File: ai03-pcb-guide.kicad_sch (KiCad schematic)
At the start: 16 parts, among them J1 Conn_01x04_Socket, J2 AVR-ISP-6, U1 ATmega32U4-A, Y1 16MHz

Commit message: more tracing work
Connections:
- net Col 11: now also U1.12 (PB7); no longer U1.25 (PD4)
- net Col 12: now also U1.25 (PD4); no longer U1.26 (PD6)
- net Col 13: now also U1.26 (PD6); no longer U1.27 (PD7)
- net Col 14: now also U1.27 (PD7); no longer U1.28 (PB4)
- net Col 2: now also U1.31 (PC6); no longer U1.12 (PB7)
- net Col 3: now also U1.32 (PC7); no longer U1.31 (PC6)
- net Col 4: now also U1.28 (PB4); no longer U1.32 (PC7)

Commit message: most wiring complete
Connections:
- net Col 0: now also U1.28 (PB4); no longer U1.29 (PB5)
- net Col 1: now also U1.29 (PB5); no longer U1.30 (PB6)
- net Col 10: now also U1.12 (PB7); no longer U1.21 (PD3)
- net Col 11: now also U1.18 (PD0); no longer U1.12 (PB7)
- net Col 12: now also U1.19 (PD1); no longer U1.25 (PD4)
- net Col 13: now also U1.21 (PD3); no longer U1.26 (PD6)
- net Col 14: now also U1.25 (PD4); no longer U1.27 (PD7)
- net Col 2: now also U1.30 (PB6); no longer U1.31 (PC6)
- net Col 3: now also U1.31 (PC6); no longer U1.32 (PC7)
- net Col 4: now also U1.32 (PC7); no longer U1.28 (PB4)
- net Col 5: now also U1.26 (PD6); no longer U1.36 (PF7)
- net Col 6: now also U1.27 (PD7); no longer U1.8 (PB0)
- net Col 7: now also U1.41 (PF0); no longer J2.1 (MISO), U1.11 (PB3)
- net Col 8: now also U1.8 (PB0); no longer U1.18 (PD0)
- net Col 9: now also J2.1 (MISO), U1.11 (PB3); no longer U1.19 (PD1)
- net Row 0: now also U1.38 (PF5); no longer U1.1 (PE6)
- net Row 1: now also U1.39 (PF4); no longer U1.37 (PF6)
- net Row 2: now also U1.40 (PF1); no longer U1.38 (PF5)
- net Row 3: now also U1.1 (PE6); no longer U1.39 (PF4)
- net Row 4: now also U1.37 (PF6); no longer U1.40 (PF1)
- net Row 5: now also U1.36 (PF7); no longer U1.41 (PF0)

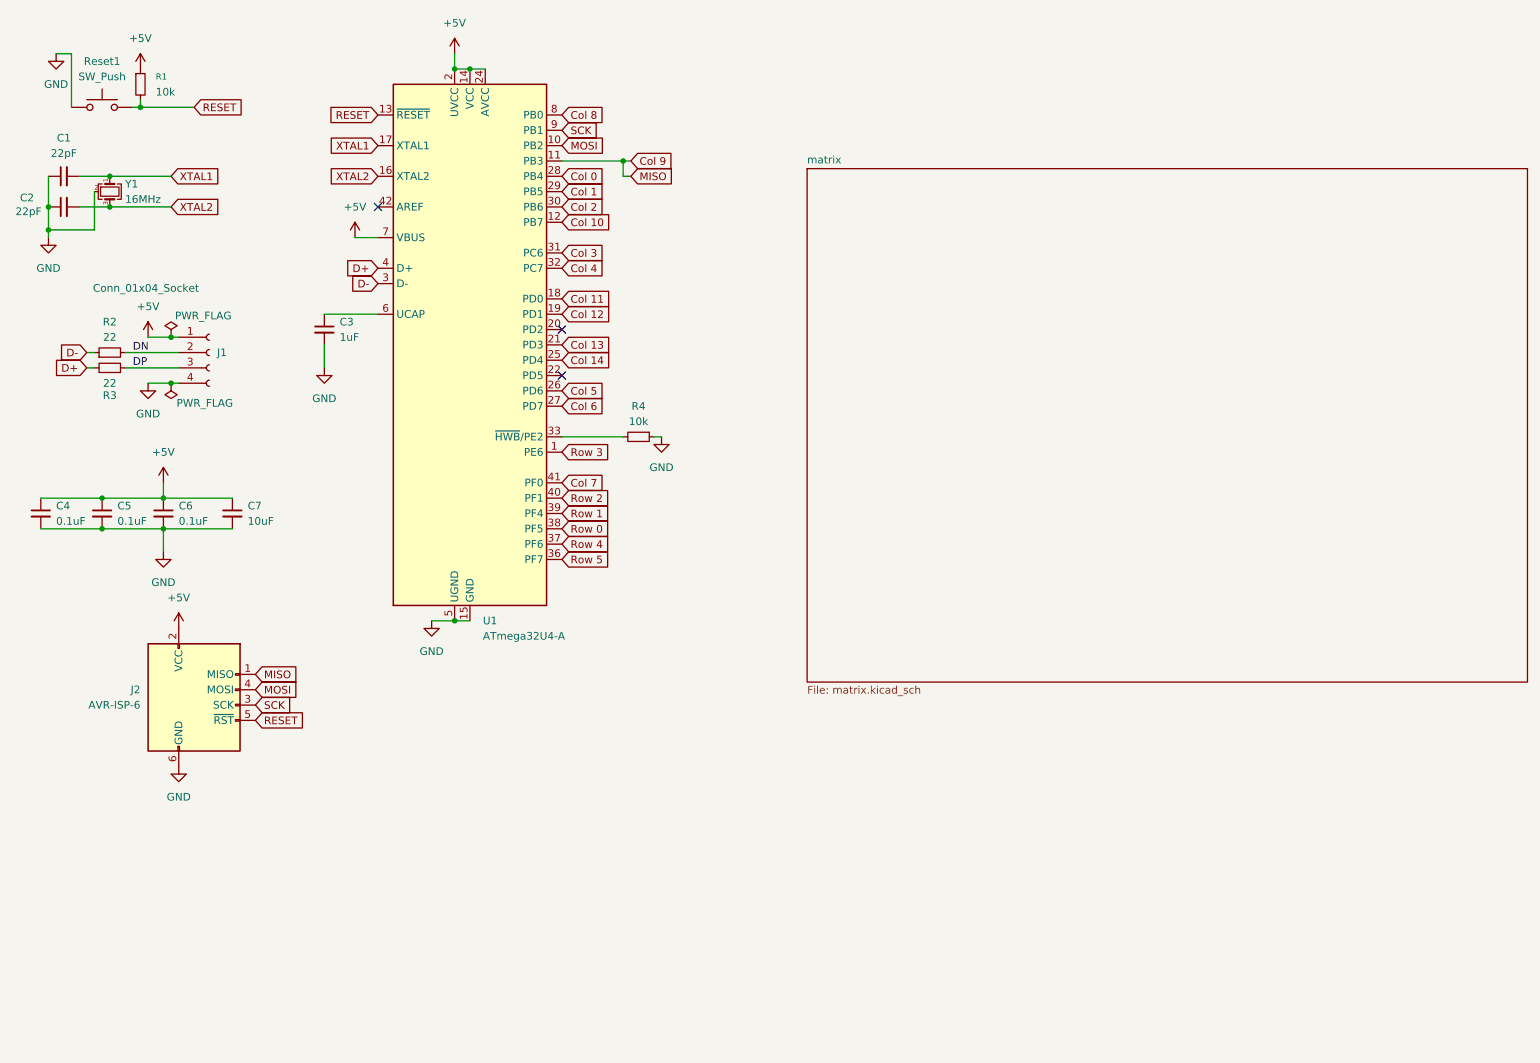
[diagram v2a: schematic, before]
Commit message: added trackpoint wiring
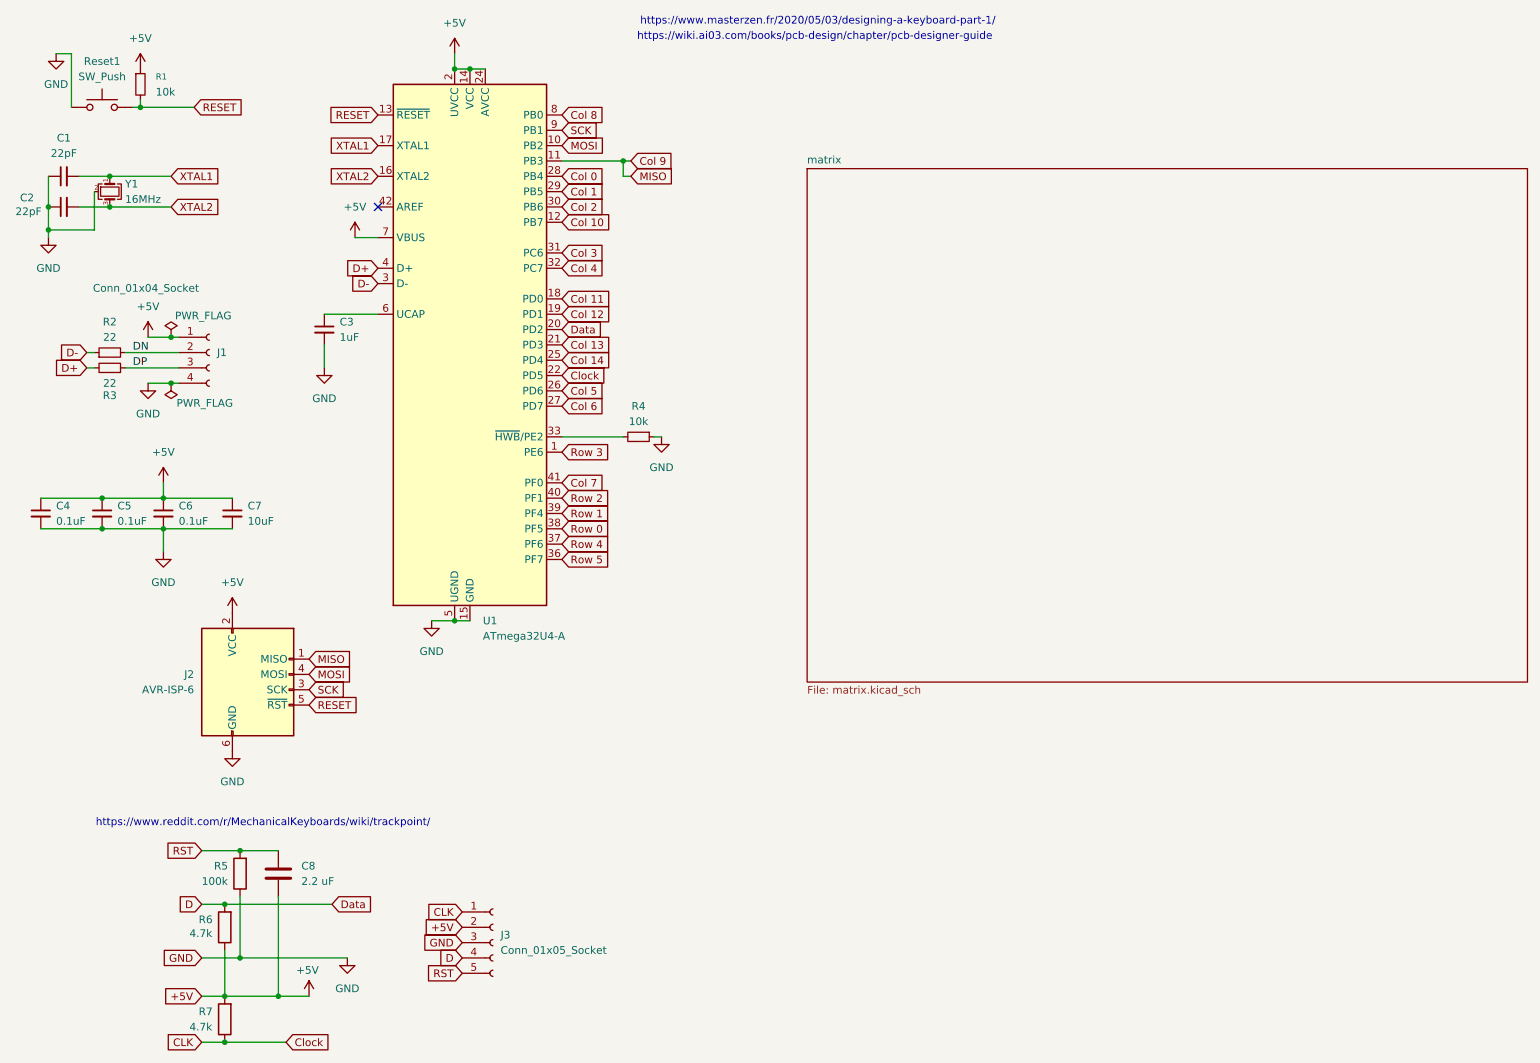
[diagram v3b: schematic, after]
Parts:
- added C8: 2.2 uF, Capacitor_SMD:C_0805_2012Metric, symbol Device:C
- added J3: Conn_01x05_Socket, Connector_Molex:Molex_Pico-EZmate_78171-0005_1x05-1MP_P1.20mm_Vertical, symbol Connector:Conn_01x05_Socket
- added R5: 100k, Resistor_SMD:R_0805_2012Metric, symbol Device:R
- added R6, R7: 4.7k, Resistor_SMD:R_0805_2012Metric, symbol Device:R
- C7: footprint Resistor_SMD:R_0805_2012Metric -> Capacitor_SMD:C_0805_2012Metric
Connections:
- net +5V: now also C8.2, J3.2 (Pin_2), R6.1, R7.2
- net GND: now also J3.3 (Pin_3), R5.1
- net D: now reaches U1.20 (PD2)
- net D: now also J3.4 (Pin_4), R6.2
- net CLK: now reaches U1.22 (PD5)
- net CLK: now also J3.1 (Pin_1), R7.1
- new net RST: C8.1, J3.5 (Pin_5), R5.2
- no-connect marks 3 -> 1
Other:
- note added: "https://wiki.ai03.com/books/pcb-design/chapter/pcb-designer-guide"
- note added: "https://www.masterzen.fr/2020/05/03/designing-a-keyboard-part-1/"
- note added: "https://www.reddit.com/r/MechanicalKeyboards/wiki/trackpoint/"
- moved on the sheet: J2

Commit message: Almost finished
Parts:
- C1, C2, C3, C4, C5, C6, C7, C8: footprint Capacitor_SMD:C_0805_2012Metric -> Capacitor_SMD:C_0603_1608Metric
- R1, R2, R3, R4, R5, R6, R7: footprint Resistor_SMD:R_0805_2012Metric -> Resistor_SMD:R_0603_1608Metric
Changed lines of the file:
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@@
 			)
 		)
-		(property "Footprint" "Resistor_SMD:R_0805_2012Metric"
+		(property "Footprint" "Resistor_SMD:R_0603_1608Metric"
 			(at 39.37 30.48 0)
 			(hide yes)
@@
 			)
 		)
-		(property "Footprint" "Capacitor_SMD:C_0805_2012Metric"
+		(property "Footprint" "Capacitor_SMD:C_0603_1608Metric"
 			(at 33.02 101.6 0)
 			(hide yes)
@@
 			)
 		)
-		(property "Footprint" "Capacitor_SMD:C_0805_2012Metric"
+		(property "Footprint" "Capacitor_SMD:C_0603_1608Metric"
 			(at 69.85 71.12 0)
 			(hide yes)
@@
 			)
 		)
-		(property "Footprint" "Resistor_SMD:R_0805_2012Metric"
+		(property "Footprint" "Resistor_SMD:R_0603_1608Metric"
 			(at 34.29 74.93 0)
 			(hide yes)
@@
 			)
 		)
-		(property "Footprint" "Capacitor_SMD:C_0805_2012Metric"
+		(property "Footprint" "Capacitor_SMD:C_0603_1608Metric"
 			(at 22.86 101.6 0)
 			(hide yes)
@@
 			)
 		)
-		(property "Footprint" "Resistor_SMD:R_0805_2012Metric"
+		(property "Footprint" "Resistor_SMD:R_0603_1608Metric"
 			(at 121.92 88.9 0)
 			(hide yes)
@@
 			)
 		)
-		(property "Footprint" "Capacitor_SMD:C_0805_2012Metric"
+		(property "Footprint" "Capacitor_SMD:C_0603_1608Metric"
 			(at 26.67 45.72 0)
 			(hide yes)
@@
 			)
 		)
-		(property "Footprint" "Capacitor_SMD:C_0805_2012Metric"
+		(property "Footprint" "Capacitor_SMD:C_0603_1608Metric"
 			(at 26.67 50.8 0)
 			(hide yes)
@@
 			)
 		)
-		(property "Footprint" "Capacitor_SMD:C_0805_2012Metric"
+		(property "Footprint" "Capacitor_SMD:C_0603_1608Metric"
 			(at 54.61 101.6 0)
 			(hide yes)
@@
 			)
 		)
-		(property "Footprint" "Resistor_SMD:R_0805_2012Metric"
+		(property "Footprint" "Resistor_SMD:R_0603_1608Metric"
 			(at 55.118 170.18 90)
 			(hide yes)
@@
 			)
 		)
-		(property "Footprint" "Capacitor_SMD:C_0805_2012Metric"
+		(property "Footprint" "Capacitor_SMD:C_0603_1608Metric"
 			(at 43.18 101.6 0)
 			(hide yes)
@@
 			)
 		)
-		(property "Footprint" "Resistor_SMD:R_0805_2012Metric"
+		(property "Footprint" "Resistor_SMD:R_0603_1608Metric"
 			(at 34.29 77.47 0)
 			(hide yes)
@@
 			)
 		)
-		(property "Footprint" "Resistor_SMD:R_0805_2012Metric"
+		(property "Footprint" "Resistor_SMD:R_0603_1608Metric"
 			(at 55.118 185.42 90)
 			(hide yes)
@@
 			)
 		)
-		(property "Footprint" "Capacitor_SMD:C_0805_2012Metric"
+		(property "Footprint" "Capacitor_SMD:C_0603_1608Metric"
 			(at 63.1952 165.1 0)
 			(hide yes)
@@
 			)
 		)
-		(property "Footprint" "Resistor_SMD:R_0805_2012Metric"
+		(property "Footprint" "Resistor_SMD:R_0603_1608Metric"
 			(at 57.658 161.29 90)
 			(hide yes)

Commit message: Rev 1.0
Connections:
- net +5V: now also J3.5 (Pin_5); no longer J3.2 (Pin_2)
- net CLK: now also J3.3 (Pin_3); no longer J3.1 (Pin_1)
- net D: now also J3.2 (Pin_2); no longer J3.4 (Pin_4)
- net GND: now also J3.1 (Pin_1); no longer J3.3 (Pin_3)
- net RST: now also J3.4 (Pin_4); no longer J3.5 (Pin_5)

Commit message: Added LCSC Part # Field
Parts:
- C1, C2: LCSC Part # (none) -> C1653
- C3: LCSC Part # (none) -> C15849
- C4, C5, C6: LCSC Part # (none) -> C14663
- C7: LCSC Part # (none) -> C19702
- C8: LCSC Part # (none) -> C1607
- J1: LCSC Part # (none) -> C588524
- J3: LCSC Part # (none) -> C724177
- R1, R4: LCSC Part # (none) -> C25804
- R2, R3: LCSC Part # (none) -> C23345
- R5: LCSC Part # (none) -> C25803
- R6, R7: LCSC Part # (none) -> C23162
- Reset1: LCSC Part # (none) -> C115351
- U1: LCSC Part # (none) -> C44854
- Y1: LCSC Part # (none) -> C12668
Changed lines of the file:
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@@
+			)
+		)
+		(property "LCSC Part #" "C724177"
+			(at 97.79 172.72 0)
+			(hide yes)
+			(show_name no)
+			(do_not_autoplace no)
+			(effects
+				(font
+					(size 1.27 1.27)
+				)
 			)
 		)
@@
 			)
 		)
+		(property "LCSC Part #" "C25804"
+			(at 39.37 30.48 0)
+			(hide yes)
+			(show_name no)
+			(do_not_autoplace no)
+			(effects
+				(font
+					(size 1.27 1.27)
+				)
+			)
+		)
 		(pin "1"
 		)
@@
 		)
 		(property "KiLib_Generator" "connector/SMD_single_row_plus_mounting_pad"
+			(at 50.8 74.93 0)
+			(hide yes)
+			(show_name no)
+			(do_not_autoplace no)
+			(effects
+				(font
+					(size 1.27 1.27)
+				)
+			)
+		)
+		(property "LCSC Part #" "C588524"
 			(at 50.8 74.93 0)
 			(hide yes)
@@
 			)
 		)
+		(property "LCSC Part #" "C14663"
+			(at 33.02 101.6 0)
+			(hide yes)
+			(show_name no)
+			(do_not_autoplace no)
+			(effects
+				(font
+					(size 1.27 1.27)
+				)
+			)
+		)
 		(pin "2"
 		)
@@
 			)
 		)
+		(property "LCSC Part #" "C15849"
+			(at 69.85 71.12 0)
+			(hide yes)
+			(show_name no)
+			(do_not_autoplace no)
+			(effects
+				(font
+					(size 1.27 1.27)
+				)
+			)
+		)
 		(pin "1"
 		)
@@
 			)
 		)
+		(property "LCSC Part #" "C23345"
+			(at 34.29 74.93 90)
+			(hide yes)
+			(show_name no)
+			(do_not_autoplace no)
+			(effects
+				(font
+					(size 1.27 1.27)
+				)
+			)
+		)
 		(pin "1"
 		)
@@
 			)
 		)
+		(property "LCSC Part #" "C14663"
+			(at 22.86 101.6 0)
+			(hide yes)
+			(show_name no)
+			(do_not_autoplace no)
+			(effects
+				(font
+					(size 1.27 1.27)
+				)
+			)
+		)
 		(pin "2"
 		)
@@
 			)
 		)
+		(property "LCSC Part #" "C25804"
+			(at 121.92 88.9 90)
+			(hide yes)
+			(show_name no)
+			(do_not_autoplace no)
+			(effects
+				(font
+					(size 1.27 1.27)
+				)
+			)
+		)
 		(pin "1"
 		)
@@
 			)
 		)
+		(property "LCSC Part #" "C1653"
+			(at 26.67 45.72 90)
+			(hide yes)
+			(show_name no)
+			(do_not_autoplace no)
+			(effects
+				(font
+					(size 1.27 1.27)
+				)
+			)
+		)
 		(pin "2"
 		)
@@
 		(property "KiLib_Generator" "SMD_2terminal_chip_molded"
 			(at 26.67 50.8 0)
+			(hide yes)
+			(show_name no)
+			(do_not_autoplace no)
+			(effects
+				(font
+					(size 1.27 1.27)
+				)
+			)
+		)
+		(property "LCSC Part #" "C1653"
+			(at 26.67 50.8 90)
 			(hide yes)
 			(show_name no)
@@
 			)
 		)
+		(property "LCSC Part #" "C19702"
+			(at 54.61 101.6 0)
+			(hide yes)
+			(show_name no)
+			(do_not_autoplace no)
+			(effects
+				(font
+					(size 1.27 1.27)
+				)
+			)
+		)
 		(pin "2"
 		)
@@
 			)
 		)
+		(property "LCSC Part #" "C115351"
+			(at 33.02 34.29 0)
+			(hide yes)
+			(show_name no)
+			(do_not_autoplace no)
+			(effects
+				(font
+					(size 1.27 1.27)
+				)
+			)
+		)
 		(pin "1"
 		)
@@
 		)
 		(property "Description" "Resistor"
+			(at 53.34 170.18 0)
+			(hide yes)
+			(show_name no)
+			(do_not_autoplace no)
+			(effects
+				(font
+					(size 1.27 1.27)
+				)
+			)
+		)
+		(property "LCSC Part #" "C23162"
 			(at 53.34 170.18 0)
 			(hide yes)
@@
 		)
 		(property "KiLib_Generator" "SMD_2terminal_chip_molded"
+			(at 43.18 101.6 0)
+			(hide yes)
+			(show_name no)
+			(do_not_autoplace no)
+			(effects
+				(font
+					(size 1.27 1.27)
+				)
+			)
+		)
+		(property "LCSC Part #" "C14663"
 			(at 43.18 101.6 0)
 			(hide yes)
@@
 			)
 		)
+		(property "LCSC Part #" "C23345"
+			(at 34.29 77.47 90)
+			(hide yes)
+			(show_name no)
+			(do_not_autoplace no)
+			(effects
+				(font
+					(size 1.27 1.27)
+				)
+			)
+		)
 		(pin "2"
 		)
@@
 			)
 		)
+		(property "LCSC Part #" "C12668"
+			(at 34.29 48.26 90)
+			(hide yes)
+			(show_name no)
+			(do_not_autoplace no)
+			(effects
+				(font
+					(size 1.27 1.27)
+				)
+			)
+		)
 		(pin "2"
 		)
@@
 			)
 		)
+		(property "LCSC Part #" "C44854 "
+			(at 93.98 73.66 0)
+			(hide yes)
+			(show_name no)
+			(do_not_autoplace no)
+			(effects
+				(font
+					(size 1.27 1.27)
+				)
+			)
+		)
 		(pin "9"
 		)
@@
 		)
 		(property "Description" "Resistor"
+			(at 53.34 185.42 0)
+			(hide yes)
+			(show_name no)
+			(do_not_autoplace no)
+			(effects
+				(font
+					(size 1.27 1.27)
+				)
+			)
+		)
+		(property "LCSC Part #" "C23162"
 			(at 53.34 185.42 0)
 			(hide yes)
@@
 			)
 		)
+		(property "LCSC Part #" "C1607"
+			(at 62.23 161.29 0)
+			(hide yes)
+			(show_name no)
+			(do_not_autoplace no)
+			(effects
+				(font
+					(size 1.27 1.27)
+				)
+			)
+		)
 		(pin "1"
 		)
@@
 			)
 		)
+		(property "LCSC Part #" ""
+			(at 57.15 130.81 0)
+			(hide yes)
+			(show_name no)
+			(do_not_autoplace no)
+			(effects
+				(font
+					(size 1.27 1.27)
+				)
+			)
+		)
 		(pin "2"
 		)
@@
 			(at 55.88 161.29 0)
 			(hide yes)
+			(show_name no)
+			(do_not_autoplace no)
+			(effects
+				(font
+					(size 1.27 1.27)
+				)
+			)
+		)
+		(property "LCSC Part #" "C25803"
+			(at 55.88 161.29 0)
+			(hide yes)
